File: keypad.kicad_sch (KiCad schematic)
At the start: 1 part, among them U5 AW9523BTQR

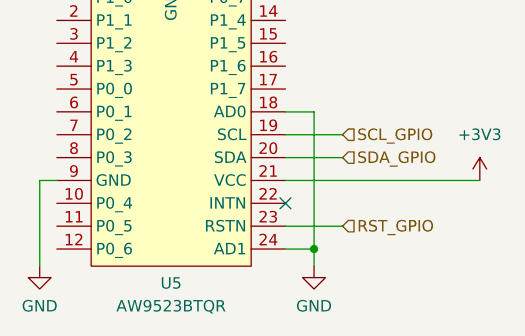
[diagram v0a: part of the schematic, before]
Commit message: USB IC Removal
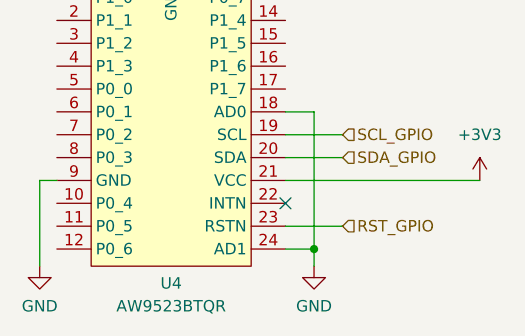
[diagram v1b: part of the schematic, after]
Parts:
- renumbered U5 to U4
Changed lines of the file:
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@@
   (symbol (lib_id "power:GND") (at 101.6 102.235 0) (unit 1)
     (in_bom yes) (on_board yes) (fields_autoplaced)
-    (property "Reference" "#PWR038" (id 0) (at 101.6 108.585 0)
+    (property "Reference" "#PWR035" (id 0) (at 101.6 108.585 0)
       (effects (font (size 1.27 1.27)) hide)
     )
@@
   (symbol (lib_id "JLCPCB:AW9523BTQR") (at 116.205 86.995 0) (unit 1)
     (in_bom yes) (on_board yes) (fields_autoplaced)
-    (property "Reference" "U5" (id 0) (at 116.205 104.14 0))
+    (property "Reference" "U4" (id 0) (at 116.205 104.14 0))
     (property "Value" "AW9523BTQR" (id 1) (at 116.205 106.68 0))
     (property "Footprint" "JLCPCB:QFN-24_EP_4x4_Pitch0.5mm" (id 2) (at 116.205 100.965 0)
@@
   (symbol (lib_id "power:+3V3") (at 150.495 92.71 0) (unit 1)
     (in_bom yes) (on_board yes) (fields_autoplaced)
-    (property "Reference" "#PWR041" (id 0) (at 150.495 96.52 0)
+    (property "Reference" "#PWR038" (id 0) (at 150.495 96.52 0)
       (effects (font (size 1.27 1.27)) hide)
     )
@@
   (symbol (lib_id "power:GND") (at 132.08 102.235 0) (unit 1)
     (in_bom yes) (on_board yes) (fields_autoplaced)
-    (property "Reference" "#PWR040" (id 0) (at 132.08 108.585 0)
+    (property "Reference" "#PWR037" (id 0) (at 132.08 108.585 0)
       (effects (font (size 1.27 1.27)) hide)
     )
@@
   (symbol (lib_id "power:GND") (at 120.015 64.135 0) (unit 1)
     (in_bom yes) (on_board yes) (fields_autoplaced)
-    (property "Reference" "#PWR039" (id 0) (at 120.015 70.485 0)
+    (property "Reference" "#PWR036" (id 0) (at 120.015 70.485 0)
       (effects (font (size 1.27 1.27)) hide)
     )

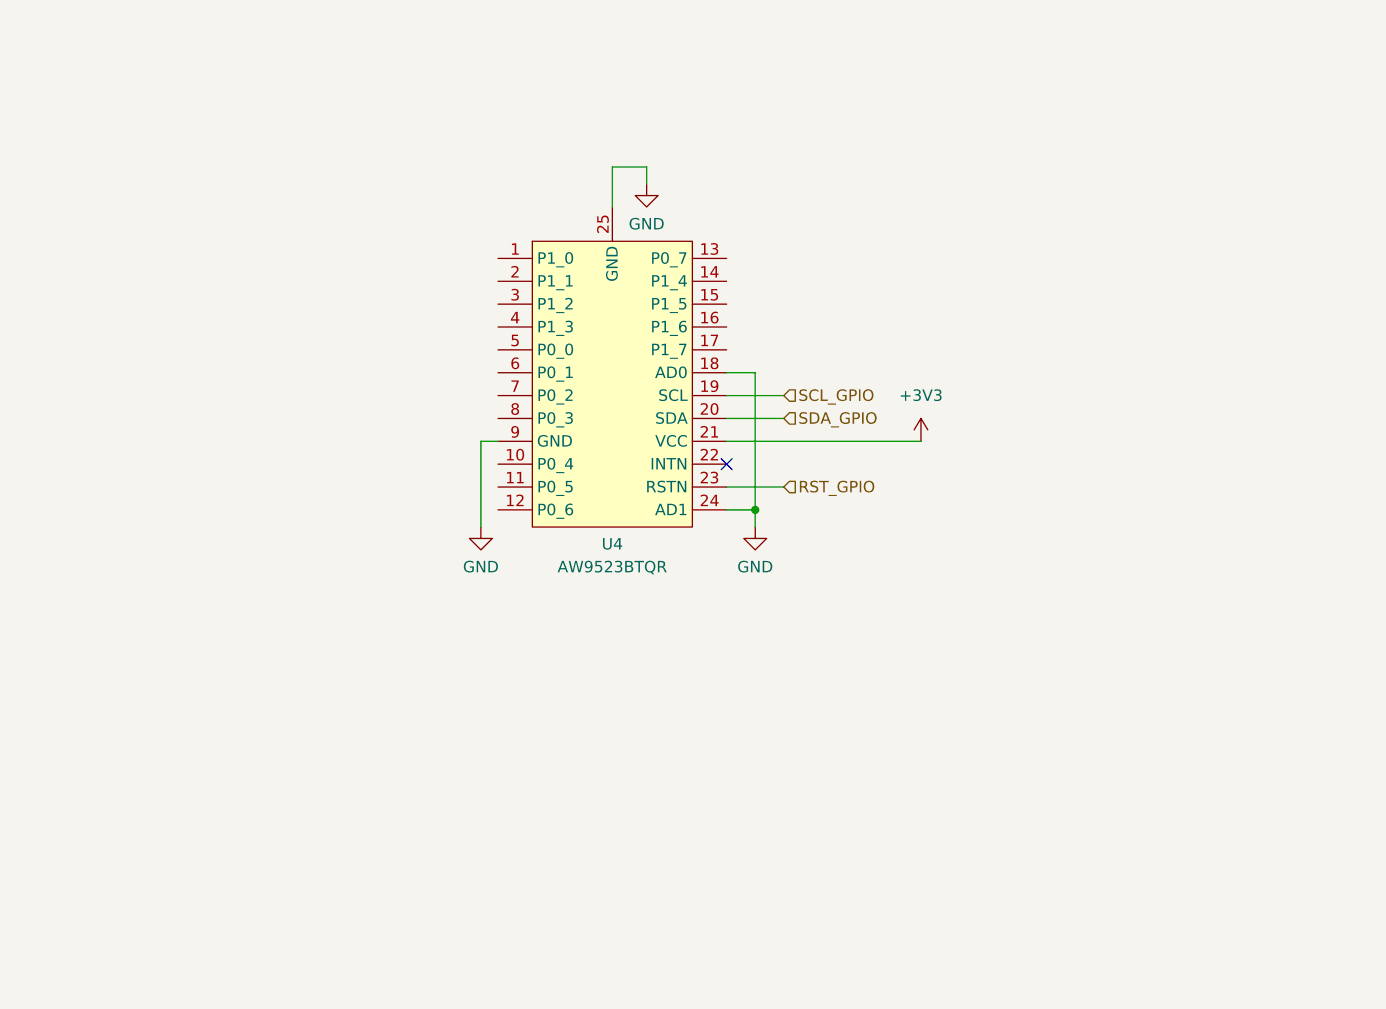
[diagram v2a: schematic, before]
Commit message: Audio near completion
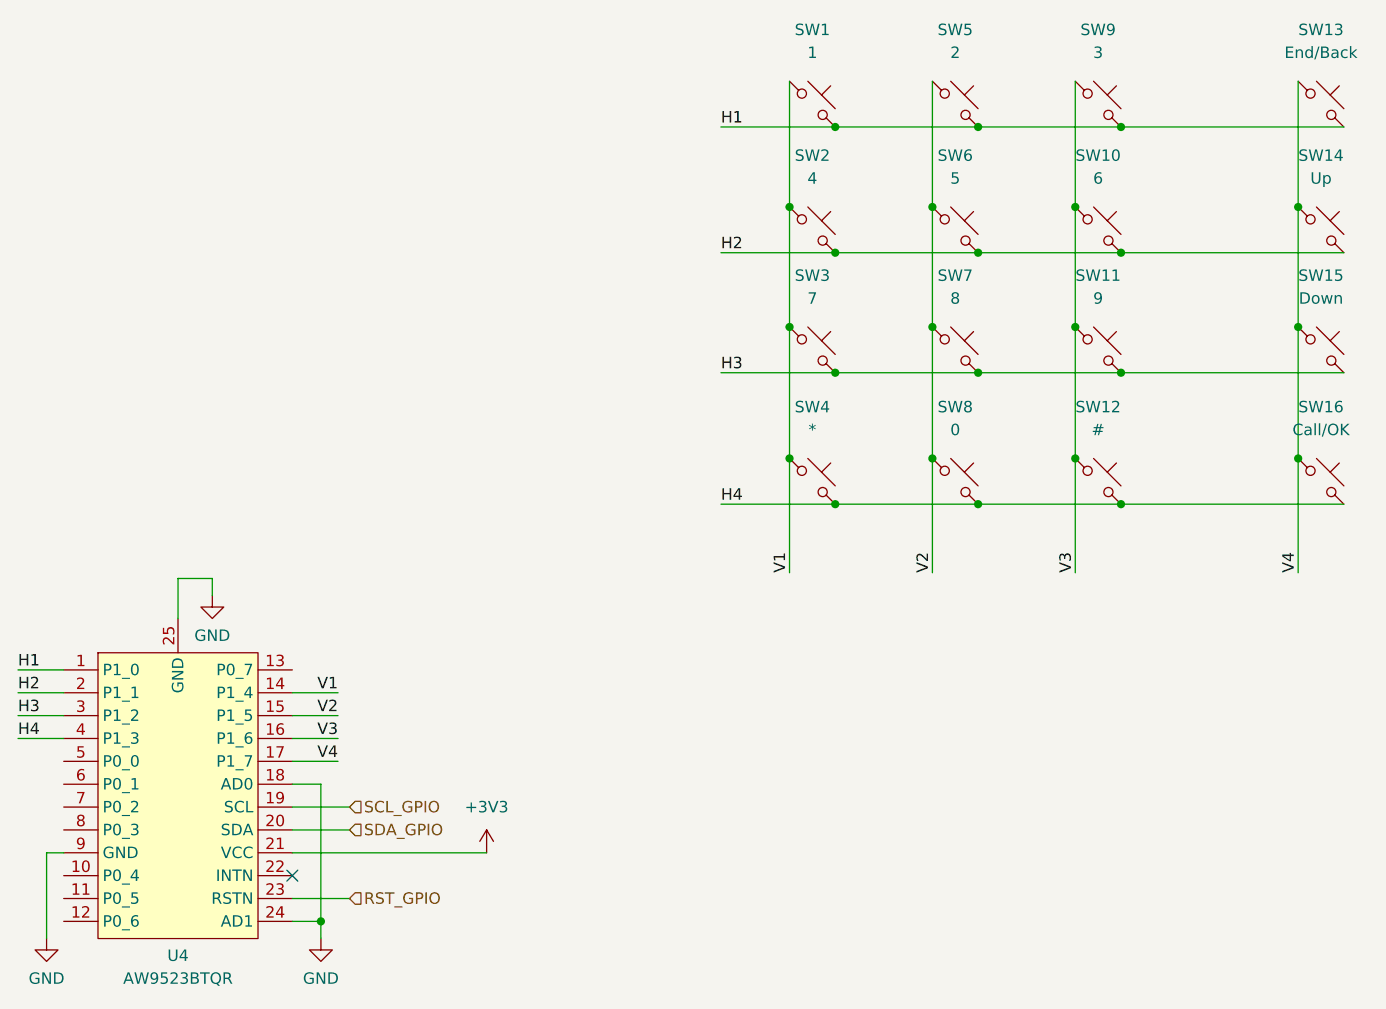
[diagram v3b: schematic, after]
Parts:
- added SW1: 1, Keypad:snap dome, symbol Switch:SW_Push_45deg
- added SW10: 6, Keypad:snap dome, symbol Switch:SW_Push_45deg
- added SW11: 9, Keypad:snap dome, symbol Switch:SW_Push_45deg
- added SW12: #, Keypad:snap dome, symbol Switch:SW_Push_45deg
- added SW13: End/Back, Keypad:snap dome, symbol Switch:SW_Push_45deg
- added SW14: Up, Keypad:snap dome, symbol Switch:SW_Push_45deg
- added SW15: Down, Keypad:snap dome, symbol Switch:SW_Push_45deg
- added SW16: Call/OK, Keypad:snap dome, symbol Switch:SW_Push_45deg
- added SW2: 4, Keypad:snap dome, symbol Switch:SW_Push_45deg
- added SW3: 7, Keypad:snap dome, symbol Switch:SW_Push_45deg
- added SW4: *, Keypad:snap dome, symbol Switch:SW_Push_45deg
- added SW5: 2, Keypad:snap dome, symbol Switch:SW_Push_45deg
- added SW6: 5, Keypad:snap dome, symbol Switch:SW_Push_45deg
- added SW7: 8, Keypad:snap dome, symbol Switch:SW_Push_45deg
- added SW8: 0, Keypad:snap dome, symbol Switch:SW_Push_45deg
- added SW9: 3, Keypad:snap dome, symbol Switch:SW_Push_45deg
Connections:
- net H1: now reaches U4.1 (P1_0)
- net H1: now also SW1.2, SW13.2, SW5.2, SW9.2
- net V1: now reaches U4.14 (P1_4)
- net V1: now also SW1.1, SW2.1, SW3.1, SW4.1
- net V2: now reaches U4.15 (P1_5)
- net V2: now also SW5.1, SW6.1, SW7.1, SW8.1
- net V3: now reaches U4.16 (P1_6)
- net V3: now also SW10.1, SW11.1, SW12.1, SW9.1
- net V4: now reaches U4.17 (P1_7)
- net V4: now also SW13.1, SW14.1, SW15.1, SW16.1
- net H2: now reaches U4.2 (P1_1)
- net H2: now also SW10.2, SW14.2, SW2.2, SW6.2
- net H3: now reaches U4.3 (P1_2)
- net H3: now also SW11.2, SW15.2, SW3.2, SW7.2
- net H4: now reaches U4.4 (P1_3)
- net H4: now also SW12.2, SW16.2, SW4.2, SW8.2
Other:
- moved on the sheet: U4

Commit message: All Routed!
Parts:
- U5: renamed from U4; footprint JLCPCB:QFN-24_EP_4x4_Pitch0.5mm -> lib_fp:QFN-24_EP_4x4_Pitch0.5mm; MPN (none) -> C148077
- renumbered SW9 to SW10, SW10 to SW11, SW11 to SW12, SW12 to SW13, SW13 to SW14, SW14 to SW15, SW15 to SW16, SW16 to SW17, SW1 to SW2, SW2 to SW3, SW3 to SW4, SW4 to SW5, SW5 to SW6, SW6 to SW7, SW7 to SW8, SW8 to SW9
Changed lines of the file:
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@@
   (symbol (lib_id "Switch:SW_Push_45deg") (at 194.945 69.215 0) (unit 1)
     (in_bom yes) (on_board yes) (fields_autoplaced)
-    (property "Reference" "SW14" (id 0) (at 194.945 60.96 0))
+    (property "Reference" "SW15" (id 0) (at 194.945 60.96 0))
     (property "Value" "Up" (id 1) (at 194.945 63.5 0))
     (property "Footprint" "Keypad:snap dome" (id 2) (at 194.945 69.215 0)
@@
   (symbol (lib_id "Switch:SW_Push_45deg") (at 154.305 82.55 0) (unit 1)
     (in_bom yes) (on_board yes) (fields_autoplaced)
-    (property "Reference" "SW7" (id 0) (at 154.305 74.295 0))
+    (property "Reference" "SW8" (id 0) (at 154.305 74.295 0))
     (property "Value" "8" (id 1) (at 154.305 76.835 0))
     (property "Footprint" "Keypad:snap dome" (id 2) (at 154.305 82.55 0)
@@
   (symbol (lib_id "power:GND") (at 53.34 147.955 0) (unit 1)
     (in_bom yes) (on_board yes) (fields_autoplaced)
-    (property "Reference" "#PWR035" (id 0) (at 53.34 154.305 0)
+    (property "Reference" "#PWR045" (id 0) (at 53.34 154.305 0)
       (effects (font (size 1.27 1.27)) hide)
     )
@@
   (symbol (lib_id "Switch:SW_Push_45deg") (at 194.945 97.155 0) (unit 1)
     (in_bom yes) (on_board yes) (fields_autoplaced)
-    (property "Reference" "SW16" (id 0) (at 194.945 88.9 0))
+    (property "Reference" "SW17" (id 0) (at 194.945 88.9 0))
     (property "Value" "Call/OK" (id 1) (at 194.945 91.44 0))
     (property "Footprint" "Keypad:snap dome" (id 2) (at 194.945 97.155 0)
@@
   (symbol (lib_id "Switch:SW_Push_45deg") (at 170.18 97.155 0) (unit 1)
     (in_bom yes) (on_board yes) (fields_autoplaced)
-    (property "Reference" "SW12" (id 0) (at 170.18 88.9 0))
+    (property "Reference" "SW13" (id 0) (at 170.18 88.9 0))
     (property "Value" "#" (id 1) (at 170.18 91.44 0))
     (property "Footprint" "Keypad:snap dome" (id 2) (at 170.18 97.155 0)
@@
   (symbol (lib_id "Switch:SW_Push_45deg") (at 138.43 82.55 0) (unit 1)
     (in_bom yes) (on_board yes) (fields_autoplaced)
-    (property "Reference" "SW3" (id 0) (at 138.43 74.295 0))
+    (property "Reference" "SW4" (id 0) (at 138.43 74.295 0))
     (property "Value" "7" (id 1) (at 138.43 76.835 0))
     (property "Footprint" "Keypad:snap dome" (id 2) (at 138.43 82.55 0)
@@
   (symbol (lib_id "Switch:SW_Push_45deg") (at 170.18 69.215 0) (unit 1)
     (in_bom yes) (on_board yes) (fields_autoplaced)
-    (property "Reference" "SW10" (id 0) (at 170.18 60.96 0))
+    (property "Reference" "SW11" (id 0) (at 170.18 60.96 0))
     (property "Value" "6" (id 1) (at 170.18 63.5 0))
     (property "Footprint" "Keypad:snap dome" (id 2) (at 170.18 69.215 0)
@@
   (symbol (lib_id "Switch:SW_Push_45deg") (at 138.43 69.215 0) (unit 1)
     (in_bom yes) (on_board yes) (fields_autoplaced)
-    (property "Reference" "SW2" (id 0) (at 138.43 60.96 0))
+    (property "Reference" "SW3" (id 0) (at 138.43 60.96 0))
     (property "Value" "4" (id 1) (at 138.43 63.5 0))
     (property "Footprint" "Keypad:snap dome" (id 2) (at 138.43 69.215 0)
@@
   (symbol (lib_id "Switch:SW_Push_45deg") (at 154.305 69.215 0) (unit 1)
     (in_bom yes) (on_board yes) (fields_autoplaced)
-    (property "Reference" "SW6" (id 0) (at 154.305 60.96 0))
+    (property "Reference" "SW7" (id 0) (at 154.305 60.96 0))
     (property "Value" "5" (id 1) (at 154.305 63.5 0))
     (property "Footprint" "Keypad:snap dome" (id 2) (at 154.305 69.215 0)
@@
   (symbol (lib_id "JLCPCB:AW9523BTQR") (at 67.945 132.715 0) (unit 1)
     (in_bom yes) (on_board yes) (fields_autoplaced)
-    (property "Reference" "U4" (id 0) (at 67.945 149.86 0))
+    (property "Reference" "U5" (id 0) (at 67.945 149.86 0))
     (property "Value" "AW9523BTQR" (id 1) (at 67.945 152.4 0))
-    (property "Footprint" "JLCPCB:QFN-24_EP_4x4_Pitch0.5mm" (id 2) (at 67.945 146.685 0)
+    (property "Footprint" "lib_fp:QFN-24_EP_4x4_Pitch0.5mm" (id 2) (at 67.945 146.685 0)
       (effects (font (size 1.27 1.27)) hide)
     )
     (property "Datasheet" "" (id 3) (at 67.945 146.685 0)
+      (effects (font (size 1.27 1.27)) hide)
+    )
+    (property "MPN" "C148077" (id 4) (at 67.945 132.715 0)
       (effects (font (size 1.27 1.27)) hide)
     )
@@
   (symbol (lib_id "power:+3V3") (at 102.235 138.43 0) (unit 1)
     (in_bom yes) (on_board yes) (fields_autoplaced)
-    (property "Reference" "#PWR038" (id 0) (at 102.235 142.24 0)
+    (property "Reference" "#PWR048" (id 0) (at 102.235 142.24 0)
       (effects (font (size 1.27 1.27)) hide)
     )
@@
   (symbol (lib_id "Switch:SW_Push_45deg") (at 170.18 82.55 0) (unit 1)
     (in_bom yes) (on_board yes) (fields_autoplaced)
-    (property "Reference" "SW11" (id 0) (at 170.18 74.295 0))
+    (property "Reference" "SW12" (id 0) (at 170.18 74.295 0))
     (property "Value" "9" (id 1) (at 170.18 76.835 0))
     (property "Footprint" "Keypad:snap dome" (id 2) (at 170.18 82.55 0)
@@
   (symbol (lib_id "Switch:SW_Push_45deg") (at 154.305 55.245 0) (unit 1)
     (in_bom yes) (on_board yes) (fields_autoplaced)
-    (property "Reference" "SW5" (id 0) (at 154.305 46.99 0))
+    (property "Reference" "SW6" (id 0) (at 154.305 46.99 0))
     (property "Value" "2" (id 1) (at 154.305 49.53 0))
     (property "Footprint" "Keypad:snap dome" (id 2) (at 154.305 55.245 0)
@@
   (symbol (lib_id "power:GND") (at 83.82 147.955 0) (unit 1)
     (in_bom yes) (on_board yes) (fields_autoplaced)
-    (property "Reference" "#PWR037" (id 0) (at 83.82 154.305 0)
+    (property "Reference" "#PWR047" (id 0) (at 83.82 154.305 0)
       (effects (font (size 1.27 1.27)) hide)
     )
@@
   (symbol (lib_id "Switch:SW_Push_45deg") (at 138.43 55.245 0) (unit 1)
     (in_bom yes) (on_board yes) (fields_autoplaced)
-    (property "Reference" "SW1" (id 0) (at 138.43 46.99 0))
+    (property "Reference" "SW2" (id 0) (at 138.43 46.99 0))
     (property "Value" "1" (id 1) (at 138.43 49.53 0))
     (property "Footprint" "Keypad:snap dome" (id 2) (at 138.43 55.245 0)
@@
   (symbol (lib_id "Switch:SW_Push_45deg") (at 154.305 97.155 0) (unit 1)
     (in_bom yes) (on_board yes) (fields_autoplaced)
-    (property "Reference" "SW8" (id 0) (at 154.305 88.9 0))
+    (property "Reference" "SW9" (id 0) (at 154.305 88.9 0))
     (property "Value" "0" (id 1) (at 154.305 91.44 0))
     (property "Footprint" "Keypad:snap dome" (id 2) (at 154.305 97.155 0)
@@
   (symbol (lib_id "power:GND") (at 71.755 109.855 0) (unit 1)
     (in_bom yes) (on_board yes) (fields_autoplaced)
-    (property "Reference" "#PWR036" (id 0) (at 71.755 116.205 0)
+    (property "Reference" "#PWR046" (id 0) (at 71.755 116.205 0)
       (effects (font (size 1.27 1.27)) hide)
     )
@@
   (symbol (lib_id "Switch:SW_Push_45deg") (at 194.945 82.55 0) (unit 1)
     (in_bom yes) (on_board yes) (fields_autoplaced)
-    (property "Reference" "SW15" (id 0) (at 194.945 74.295 0))
+    (property "Reference" "SW16" (id 0) (at 194.945 74.295 0))
     (property "Value" "Down" (id 1) (at 194.945 76.835 0))
     (property "Footprint" "Keypad:snap dome" (id 2) (at 194.945 82.55 0)
@@
   (symbol (lib_id "Switch:SW_Push_45deg") (at 170.18 55.245 0) (unit 1)
     (in_bom yes) (on_board yes) (fields_autoplaced)
-    (property "Reference" "SW9" (id 0) (at 170.18 46.99 0))
+    (property "Reference" "SW10" (id 0) (at 170.18 46.99 0))
     (property "Value" "3" (id 1) (at 170.18 49.53 0))
     (property "Footprint" "Keypad:snap dome" (id 2) (at 170.18 55.245 0)
@@
   (symbol (lib_id "Switch:SW_Push_45deg") (at 194.945 55.245 0) (unit 1)
     (in_bom yes) (on_board yes) (fields_autoplaced)
-    (property "Reference" "SW13" (id 0) (at 194.945 46.99 0))
+    (property "Reference" "SW14" (id 0) (at 194.945 46.99 0))
     (property "Value" "End/Back" (id 1) (at 194.945 49.53 0))
     (property "Footprint" "Keypad:snap dome" (id 2) (at 194.945 55.245 0)
@@
   (symbol (lib_id "Switch:SW_Push_45deg") (at 138.43 97.155 0) (unit 1)
     (in_bom yes) (on_board yes) (fields_autoplaced)
-    (property "Reference" "SW4" (id 0) (at 138.43 88.9 0))
+    (property "Reference" "SW5" (id 0) (at 138.43 88.9 0))
     (property "Value" "*" (id 1) (at 138.43 91.44 0))
     (property "Footprint" "Keypad:snap dome" (id 2) (at 138.43 97.155 0)
